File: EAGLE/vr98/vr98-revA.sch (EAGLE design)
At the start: 310 parts, among them U1 STM32F411CEU7

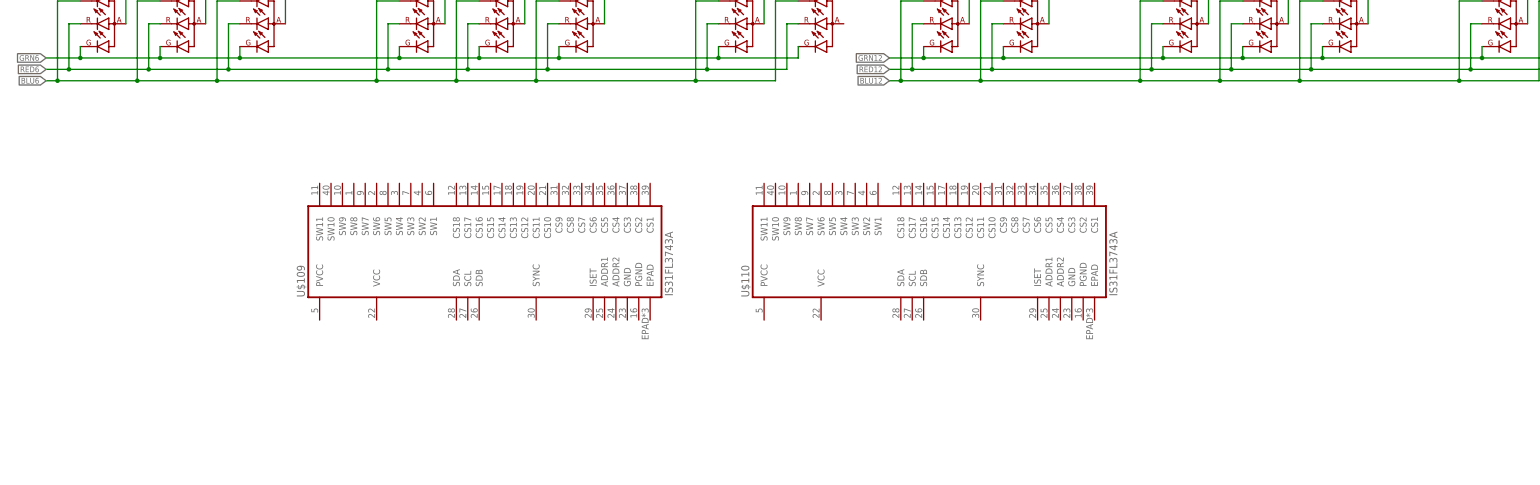
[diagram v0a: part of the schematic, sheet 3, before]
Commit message: led matrix done
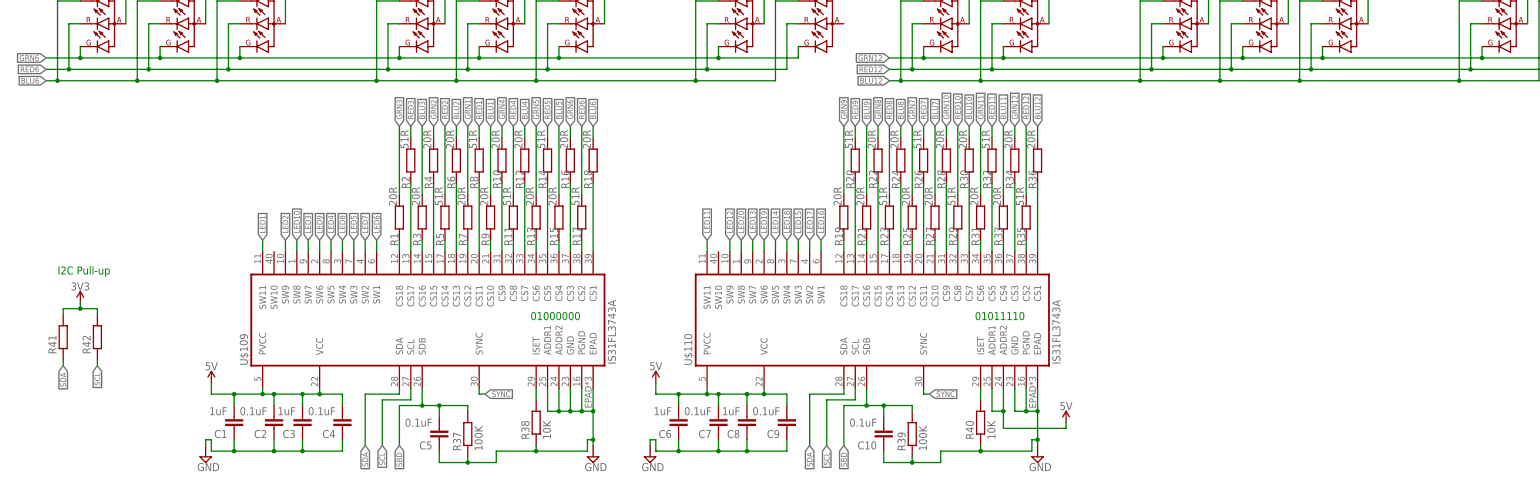
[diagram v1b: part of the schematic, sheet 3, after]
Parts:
- added C1, C3, C6, C8: 1uF, rcl:C-EUC0603
- added C10, C2, C4, C5, C7, C9: 0.1uF, rcl:C-EUC0603
- added R1, R10, R12, R13, R15, R16, R18, R19, R21, R22, R24, R25, R27, R28, R3, R30, R31, R33, R34, R36, R4, R6, R7, R9: 20R, rcl:R-EU_R0603
- added R11, R14, R17, R2, R20, R23, R26, R29, R32, R35, R5, R8: 51R, rcl:R-EU_R0603
- added R37, R39: 100K, rcl:R-EU_R0603
- added R38, R40: 10K, rcl:R-EU_R0603
- added R41, R42: (no value), rcl:R-EU_R0603
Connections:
- new net GND: C1.1, C10.1, C2.1, C3.1, C4.1, C5.1, C6.1, C7.1, C8.1, C9.1, R37.1, R38.1, R39.1, R40.1, U$109.ADDR1, U$109.ADDR2, U$109.EPAD, U$109.GND, U$109.PGND, U$110.EPAD, U$110.GND, U$110.PGND
- new net N$10: R29.1, U$110.CS8
- new net N$11: R28.1, U$110.CS9
- new net N$12: R27.1, U$110.CS10
- new net N$123: R14.1, U$109.CS5
- new net N$124: R13.1, U$109.CS6
- new net N$125: R12.1, U$109.CS7
- new net N$126: R11.1, U$109.CS8
- new net N$127: R10.1, U$109.CS9
- new net N$128: R9.1, U$109.CS10
- new net N$129: R8.1, U$109.CS11
- new net N$13: R26.1, U$110.CS11
- new net N$130: R7.1, U$109.CS12
- new net N$131: R5.1, U$109.CS14
- new net N$132: R4.1, U$109.CS15
- new net N$133: R3.1, U$109.CS16
- new net N$134: R2.1, U$109.CS17
- new net N$135: R1.1, U$109.CS18
- new net N$136: R38.2, U$109.ISET
- new net N$137: R40.2, U$110.ISET
- new net N$14: R25.1, U$110.CS12
- new net N$15: R23.1, U$110.CS14
- new net N$153: R6.1, U$109.CS13
- new net N$16: R22.1, U$110.CS15
- new net N$17: R21.1, U$110.CS16
- new net N$18: R20.1, U$110.CS17
- new net N$19: R19.1, U$110.CS18
- new net N$20: R24.1, U$110.CS13
- new net N$21: R18.1, U$109.CS1
- new net N$22: R17.1, U$109.CS2
- new net N$23: R16.1, U$109.CS3
- new net N$24: R15.1, U$109.CS4
- new net N$3: R36.1, U$110.CS1
- new net N$4: R35.1, U$110.CS2
- new net N$5: R34.1, U$110.CS3
- new net N$6: R33.1, U$110.CS4
- new net N$7: R32.1, U$110.CS5
- new net N$8: R31.1, U$110.CS6
- new net N$9: R30.1, U$110.CS7
- new net SBD: C10.2, C5.2, R37.2, R39.2, U$109.SDB, U$110.SDB
- new net SCL: R42.1, U$109.SCL, U$110.SCL
- new net SDA: R41.1, U$109.SDA, U$110.SDA
- new net SYNC: U$109.SYNC, U$110.SYNC
- new net VCC_1: C1.2, C2.2, C3.2, C4.2, C6.2, C7.2, C8.2, C9.2, U$109.PVCC, U$109.VCC, U$110.ADDR1, U$110.ADDR2, U$110.PVCC, U$110.VCC
- new net VCC_2: R41.2, R42.2
- net BLU1: now also R9.2
- net BLU10: now also R30.2
- net BLU11: now also R33.2
- net BLU12: now also R36.2
- net BLU2: now also R6.2
- net BLU3: now also R3.2
- net BLU4: now also R12.2
- net BLU5: now also R15.2
- net BLU6: now also R18.2
- net BLU7: now also R27.2
- net BLU8: now also R24.2
- net BLU9: now also R21.2
- net GRN1: now also R7.2
- net GRN10: now also R28.2
- net GRN11: now also R31.2
- net GRN12: now also R34.2
- net GRN2: now also R4.2
- net GRN3: now also R1.2
- net GRN4: now also R10.2
- net GRN5: now also R13.2
- net GRN6: now also R16.2
- net GRN7: now also R25.2
- net GRN8: now also R22.2
- net GRN9: now also R19.2
- net LED1: now also U$109.SW11
- net LED10: now also U$109.SW8
- net LED11: now also U$110.SW11
- net LED12: now also U$110.SW9
- net LED13: now also U$110.SW7
- net LED14: now also U$110.SW5
- net LED15: now also U$110.SW3
- net LED16: now also U$110.SW1
- net LED17: now also U$110.SW2
- net LED18: now also U$110.SW4
- net LED19: now also U$110.SW6
- net LED2: now also U$109.SW9
- net LED20: now also U$110.SW8
- net LED3: now also U$109.SW7
- net LED4: now also U$109.SW5
- net LED5: now also U$109.SW3
- net LED6: now also U$109.SW1
- net LED7: now also U$109.SW2
- net LED8: now also U$109.SW4
- net LED9: now also U$109.SW6
- net RED1: now also R8.2
- net RED10: now also R29.2
- net RED11: now also R32.2
- net RED12: now also R35.2
- net RED2: now also R5.2
- net RED3: now also R2.2
- net RED4: now also R11.2
- net RED5: now also R14.2
- net RED6: now also R17.2
- net RED7: now also R26.2
- net RED8: now also R23.2
- net RED9: now also R20.2
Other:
- note added: "01000000"
- note added: "01011110"
- note added: "I2C Pull-up"
- moved on the sheet: U$109, U$110

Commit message: wip
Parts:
- added C11: 22uF, rcl:C-EUC0603
- added C12, C13, C14, C15: 100nF, rcl:C-EUC0603
- added C16, C17, C18, C19: (no value), rcl:C-EUC0603
- added C20, C21, C25, C26, C27: 100nF, SparkFun-Capacitors:0.1UF-0603-25V-5%
- added C22, C23: 22uF, SparkFun-Capacitors:0.22UF-0603-25V-10%
- added C24: 4.7uF, SparkFun-Capacitors:1.0NF/1000PF-0603-50V-10%
- added D00: B5819W SL, jlcpcb_basic_parts:1N5819WS
- added D101, D102, D103: (no value), jlcpcb_basic_parts:1N5819WS
- added J1: (no value), ts_keyboards:UBD-C3
- added J2: (no value), ts_keyboards:UBD-S1_C4
- added L1: 10uH ±10%, rcl:L-USL3225M
- added LM1117: AMS1117-3.3, SparkFun-IC-Power:V_REG_LM1117SOT223
- added R43, R44: 5.1K, rcl:R-EU_R0603
- added R45, R46: 10R, rcl:R-EU_R0603
- added SW_CL_2, SW_SPC_2, SW_SPC_3: MX-5-PIN-MILMAX-3305-XNO-SILK, ts_keyboards:MX-5-PIN-MILMAX-3305-XNO-SILK
- added SW_DP_2, SW_ENT_2, SW_F17_2, SW_LS_2, SW_NUBS: MX-5-PIN-HOTSWAP-PADNO-SILK, ts_keyboards:MX-5-PIN-HOTSWAP-PADNO-SILK
- added U$108: DNP, ts_keyboards:156120M173000
- added U$111: M25C, ts_kb_mcu:M25C
- added U2, U3, U4: 74HC595PW, __untitled:74HC595PW
- added Y1: 32.768kHz ±20ppm 6pF, SparkFun-Clocks:CRYSTAL-32.768KHZSMD-3.2X1.5
- added Y2: 25MHz 9pF, SparkFun-Clocks:CRYSTAL-24MHZ"
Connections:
- net N$79 renamed K_CL
- new net ENC_A: R44.1, SW_F17.A, U1A.PA8
- new net ENC_B: R43.1, SW_F17.B, U1A.PA9
- new net K_DP: D50.A, SW_DP.P, SW_DP_2.P
- new net K_ENT: D67.A, SW_ENT.P, SW_ENT_2.P
- new net K_F13: D18.A, SW_F17.D, SW_F17_2.P
- new net K_LS: D71.A, SW_CL_2.P, SW_LS.P, SW_LS_2.P
- new net MISO: U1A.PA6
- new net MOSI: U1A.PA7
- new net N$138: C18.1, U1A.PH0-OSC_IN, Y2.2
- new net N$139: C19.1, U1A.PH1-OSC_OUT, Y2.1
- new net N$140: R45.2, U1A.PA11
- new net N$141: R46.2, U1A.PA12
- new net N$142: D101.A, SW_NUBS.P
- new net N$154: D102.A, SW_SPC_2.P
- new net N$155: D103.A, SW_SPC_3.P
- new net N$79: C16.1, U1A.PC14-OSC32_IN, Y1.2
- new net SCKL: U1A.PA5
- new net UDB_DP: R46.1
- new net USB_DN: J1.D-, J2.D-, R45.1
- new net USB_DP: J1.D+, J2.D+
- net BLU7: now also U$108.B
- net COL0: now also SW_CL_2.S, SW_LS_2.S
- net COL1: now also SW_NUBS.S
- net COL13: now also SW_DP_2.S, SW_ENT_2.S
- net COL17: now also SW_F17_2.S
- net COL3: now also SW_SPC_2.S
- net COL7: now also SW_SPC_3.S
- net GND: now also C11.2, C12.2, C13.2, C14.2, C15.2, C16.2, C17.2, C18.2, C19.2, C20.2, C21.2, C22.2, C23.2, C24.2, J1.GND, J2.GND, LM1117.ADJ, SW_F17.1, SW_F17.2, SW_F17.C, U1B.EPAD, U1B.VSS, U1B.VSSA, U1B.VSS_2, U1B.VSS_3
- net GRN7: now also U$108.G
- net LED20: now also U$108.A
- net N$1: now also L1.1, U1B.VREF+; no longer D71.A, SW_LS.P
- net N$122: now also C17.1, U1A.PC15-OSC32_OUT, Y1.1; no longer D18.A, SW_F17.D
- net N$70: now also C13.1, C14.1, C15.1; no longer D50.A, SW_DP.P
- net N$75: now also C11.1, U1B.VCAP1; no longer D67.A, SW_ENT.P
- net RED7: now also U$108.R
- net ROW4: now also D101.C
- net ROW5: now also D102.C, D103.C
- net SCL: now also U1A.PB6
- net SDA: now also U1A.PB7
- net VCC_1: now also C21.1, C23.1, D00.C, J1.VCC, J2.VCC, LM1117.IN
- net VCC_2: now also C12.1, C20.1, C22.1, C24.1, D00.A, L1.2, LM1117.OUT, R43.2, R44.2, U1B.VDD, U1B.VDD_2, U1B.VDD_3
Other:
- note added: "** NEW ** Unified Daughter Board (C4) Conn."
- note added: "DNP"
- note added: "DNP Unified Daughter Board (C3) Conn."
- moved on the sheet: U1A, U1B

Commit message: wip
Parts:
- removed SW_F17_2: MX-5-PIN-HOTSWAP-PADNO-SILK, ts_keyboards:MX-5-PIN-HOTSWAP-PADNO-SILK
- removed U$111: M25C, ts_kb_mcu:M25C
- added C28: 100nF, SparkFun-Capacitors:0.1UF-0603-25V-5%
- added C29: (no value), rcl:C-EUC0603
- added C30: 100nF, rcl:C-EUC0805
- added C31: 100nF, rcl:C-EUC0603
- added D104: (no value), jlcpcb_basic_parts:1N5819WS
- added D107: BLUE, SparkFun-LED:LED-BLUE0603
- added D201, D202: 1N4148, adafruit:DIODESOT23_REFLOW
- added JI2C, JPWM: (no value), SparkFun-Connectors:CONN_04
- added JKEY: (no value), __untitled:MOLEX_0781710004
- added JSPI: DNP, SparkFun-Connectors:AVR_SPI_PROG_3X2NS
- added JSPI@2: (no value), SparkFun-Connectors:CONN_01
- added JTAG: DNP, SparkFun-Connectors:CONN_05X2NO_SILK
- added J_5V: 5V SRC SELECT, SparkFun-Jumpers:JUMPER-SMT_3_1-NC_TRACE_SILK
- added Q1: 2N7002, adafruit:MOSFET-NREFLOW
- added Q2: DMG2305UX-7, SparkFun-DiscreteSemi:MOSFET_PCH-DMG2305UX-7
- added Q3: IRLML6401, SparkFun-DiscreteSemi:MOSFET_PCH-IRLML2244
- added Q4: 2N2222, SparkFun-DiscreteSemi:TRANS_NPN-MMBT2222AL
- added R47, R48, R49, R50, R51, R52, R53, R54, R55, R56, R57, R58, R59, R60, R61, R62, R63, R64, R66: 10K, rcl:R-EU_R0603
- added R65: 5.1K, rcl:R-EU_R0603
- added R67, R68, R71, R73: 100K, rcl:R-EU_R0603
- added R69: /DNP/, rcl:R-EU_R0603
- added R70, R72: 1K, rcl:R-EU_R0603
- added S1: Reset, SparkFun-Switches:MOMENTARY-SWITCH-SPST-SMD-5.2-TALL-REDUNDANT
- added S2: KEY, SparkFun-Switches:MOMENTARY-SWITCH-SPST-SMD-5.2-TALL-REDUNDANT
- added SW_F13_2: MX-5-PIN-HOTSWAP-PADNO-SILK, ts_keyboards:MX-5-PIN-HOTSWAP-PADNO-SILK
- added U5: M25C, ts_kb_mcu:M25C
- C16, C17: value (none) -> 4.3pF
- C18, C19: value (none) -> 12pF
- D102: value (none) -> DNP
- U2, U3, U4: value 74HC595PW -> 74HC589A_DT; device __untitled:74HC595PW -> __untitled:74HC589A_DT
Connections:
- net N$54 renamed K_BSP
- removed net N$1: L1.1, U1B.VREF+
- removed net SCKL: U1A.PA5
- new net !BOOT: C30.1, D202.A, Q2.G, R67.1
- new net !RESET: C29.2, D201.A, R69.1, U1A.NRST
- new net 5V_SELECT: C1.2, C2.2, C3.2, C4.2, C6.2, C7.2, C8.2, C9.2, J_5V.2, U$109.PVCC, U$109.VCC, U$110.ADDR1, U$110.ADDR2, U$110.PVCC, U$110.VCC
- new net AUX_CS: JSPI.5, U1A.PB1
- new net AUX_DC: JSPI@2.1, U1A.PA1
- new net BOOT0: Q2.D, R68.1, U1A.BOOT0
- new net BOOT1: R66.2, U1A.PB2
- new net CK/DATA/PWM: JPWM.3, U1A.PA8
- new net EE_CS: U1A.PB0, U5.!CS
- new net GND2: R47.1, R48.1, R49.1, R50.1, R51.1, R52.1, R53.1, R54.1, R55.1, R56.1, R57.1, R58.1, R59.1, R60.1, R61.1, R62.1, R63.1, R64.1
- new net J_RST: JTAG.10, U1A.PB4
- new net J_TCK: JTAG.4, U1A.PA14
- new net J_TDI: JTAG.8, U1A.PA15
- new net J_TDO: JTAG.6, U1A.PB3
- new net J_TMS: JTAG.2, U1A.PA13
- new net LATCH: Q1.D, R65.1, U2.LATCH, U2.SS/!PL, U3.LATCH, U3.SS/!PL, U4.LATCH, U4.SS/!PL
- new net LED: D107.C, U1A.PC13-ANTI_TAMP
- new net LED_EN: R73.2, U1A.PB10
- new net LED_VCC: C31.1, J_5V.1, Q3.D
- new net MATRIX_CS: Q1.G, U1A.PA4, U2.OE/!CS, U3.OE/!CS, U4.OE/!CS
- new net N$143: C12.1, L1.1, U1B.VREF+
- new net N$144: D102.A, JKEY.3, S2.1
- new net N$145: D107.A, R70.2
- new net N$146: D201.C, D202.C, S1.2
- new net N$147: Q4.C, R72.1
- new net N$148: C31.2, Q3.G, R71.1, R72.2
- new net N$149: U3.QH, U4.SA
- new net N$162: U2.QH, U3.SA
- new net N$54: Q1.S
- new net RX: U1A.PA10
- new net SCK: JSPI.3, U1A.PA5, U2.SC/SCK, U3.SC/SCK, U4.SC/SCK, U5.CLK
- new net TX: U1A.PA9
- new net WKUP: U1A.PA0-WKUP
- net COL0: now also D1.C, D19.C, D37.C, D55.C, D71.C, D88.C, R47.2, U2.B; no longer SW_CL.S, SW_CL_2.S, SW_ESC.S, SW_LC.S, SW_LS.S, SW_LS_2.S, SW_TAB.S, SW_TDL.S
- net COL1: now also D2.C, D20.C, D38.C, D56.C, D89.C, R48.2, U2.C; no longer SW_1.S, SW_A.S, SW_F1.S, SW_LW.S, SW_NUBS.S, SW_Q.S
- net COL10: now also D11.C, D29.C, D47.C, D65.C, D80.C, D95.C, R57.2, U3.F; no longer SW_0.S, SW_CS.S, SW_DT.S, SW_F10.S, SW_P.S, SW_RC.S
- net COL11: now also D12.C, D30.C, D48.C, D66.C, D81.C, R58.2, U3.G; no longer SW_F11.S, SW_FN.S, SW_FS.S, SW_MU.S, SW_OB.S, SW_QU.S
- net COL12: now also D13.C, D31.C, D49.C, D82.C, D96.C, R59.2, U4.B; no longer SW_CB.S, SW_EP.S, SW_F12.S, SW_LF.S, SW_RS.S
- net COL13: now also D14.C, D32.C, D50.C, D67.C, D83.C, D97.C, R60.2, SW_DP_2.P, SW_ENT_2.P, U4.C; no longer SW_BSP.S, SW_DN.S, SW_DP.S, SW_DP_2.S, SW_ENT.S, SW_ENT_2.S, SW_F13.S, SW_UP.S
- net COL14: now also D15.C, D33.C, D51.C, D68.C, D84.C, D98.C, R61.2, U4.D; no longer SW_F14.S, SW_N1.S, SW_N4.S, SW_N7.S, SW_NUM.S, SW_RT.S
- net COL15: now also D16.C, D34.C, D52.C, D69.C, D85.C, D99.C, R62.2, U4.E; no longer SW_DSH.S, SW_F15.S, SW_N0.S, SW_N2.S, SW_N5.S, SW_N8.S
- net COL16: now also D100.C, D17.C, D35.C, D53.C, D70.C, D86.C, R63.2, U4.F; no longer SW_F16.S, SW_MUL.S, SW_N3.S, SW_ND.S
- net COL17: now also D18.C, D36.C, D54.C, D87.C, R64.2, SW_F13_2.P, U4.G; no longer SW_F17.E, SW_F17_2.S, SW_MIN.S, SW_NEN.S, SW_NP.S
- net COL2: now also D101.C, D21.C, D3.C, D39.C, D57.C, D72.C, D90.C, R49.2, U2.D; no longer SW_2.S, SW_F2.S, SW_LA.S, SW_S.S, SW_W.S, SW_Z.S
- net COL3: now also D103.C, D22.C, D4.C, D40.C, D58.C, D73.C, R50.2, U2.E; no longer SW_3.S, SW_D.S, SW_E.S, SW_F3.S, SW_SPC_2.S, SW_X.S
- net COL4: now also D102.C, D23.C, D41.C, D5.C, D59.C, D74.C, R51.2, U2.F; no longer SW_4.S, SW_C.S, SW_F.S, SW_F4.S, SW_R.S
- net COL5: now also D24.C, D42.C, D6.C, D60.C, D75.C, D91.C, R52.2, U2.G; no longer SW_5.S, SW_F5.S, SW_G.S, SW_SPC.S, SW_T.S, SW_V.S
- net COL6: now also D104.C, D25.C, D43.C, D61.C, D7.C, D76.C, R53.2, U3.B; no longer SW_6.S, SW_B.S, SW_F6.S, SW_H.S, SW_Y.S
- net COL7: now also D26.C, D44.C, D62.C, D77.C, D8.C, D92.C, R54.2, U3.C; no longer SW_7.S, SW_F7.S, SW_J.S, SW_N.S, SW_SPC_3.S, SW_U.S
- net COL8: now also D27.C, D45.C, D63.C, D78.C, D9.C, D93.C, R55.2, U3.D; no longer SW_8.S, SW_F8.S, SW_I.S, SW_K.S, SW_M.S, SW_RA.S
- net COL9: now also D10.C, D28.C, D46.C, D64.C, D79.C, D94.C, R56.2, U3.E; no longer SW_9.S, SW_CM.S, SW_F9.S, SW_L.S, SW_O.S, SW_RW.S
- net ENC_A: now also U1A.PA2; no longer U1A.PA8
- net ENC_B: now also U1A.PA3; no longer U1A.PA9
- net GND: now also C25.2, C26.2, C27.2, C28.2, C29.1, C30.2, JI2C.4, JKEY.4, JPWM.4, JSPI.6, JTAG.3, JTAG.5, JTAG.9, Q4.E, R66.1, R68.2, S1.1, U1B.VBAT, U2.A, U2.GND, U2.H, U2.SA, U3.A, U3.GND, U3.H, U4.A, U4.GND, U4.H, U5.GND
- net K_CL: now also SW_CL_2.P
- net K_DP: now also SW_DP_2.S; no longer SW_DP_2.P
- net K_ENT: now also SW_ENT_2.S; no longer SW_ENT_2.P
- net K_F13: now also SW_F13_2.S; no longer SW_F17_2.P
- net K_LS: no longer SW_CL_2.P
- net LED10: now also U$100.A
- net MISO: now also JSPI.1, U4.QH, U5.DO
- net MOSI: now also JSPI.4, U5.DIO
- net N$154: now also D103.A; no longer D102.A
- net N$155: now also D104.A; no longer D103.A
- net N$70: now also Q4.B, R73.1; no longer C13.1, C14.1, C15.1
- net ROW0: now also SW_ESC.S, SW_F1.S, SW_F10.S, SW_F11.S, SW_F12.S, SW_F13.S, SW_F14.S, SW_F15.S, SW_F16.S, SW_F17.E, SW_F2.S, SW_F3.S, SW_F4.S, SW_F5.S, SW_F6.S, SW_F7.S, SW_F8.S, SW_F9.S, U1A.PB12; no longer D1.C, D10.C, D11.C, D12.C, D13.C, D14.C, D15.C, D16.C, D17.C, D18.C, D2.C, D3.C, D4.C, D5.C, D6.C, D7.C, D8.C, D9.C
- net ROW1: now also SW_0.S, SW_1.S, SW_2.S, SW_3.S, SW_4.S, SW_5.S, SW_6.S, SW_7.S, SW_8.S, SW_9.S, SW_BSP.S, SW_DSH.S, SW_EP.S, SW_MIN.S, SW_MU.S, SW_MUL.S, SW_NUM.S, SW_TDL.S, U1A.PB13; no longer D19.C, D20.C, D21.C, D22.C, D23.C, D24.C, D25.C, D26.C, D27.C, D28.C, D29.C, D30.C, D31.C, D32.C, D33.C, D34.C, D35.C, D36.C
- net ROW2: now also SW_CB.S, SW_DP.S, SW_E.S, SW_I.S, SW_N7.S, SW_N8.S, SW_N9.S, SW_NP.S, SW_O.S, SW_OB.S, SW_P.S, SW_Q.S, SW_R.S, SW_T.S, SW_TAB.S, SW_U.S, SW_W.S, SW_Y.S, U1A.PB14; no longer D37.C, D38.C, D39.C, D40.C, D41.C, D42.C, D43.C, D44.C, D45.C, D46.C, D47.C, D48.C, D49.C, D50.C, D51.C, D52.C, D53.C, D54.C
- net ROW3: now also SW_A.S, SW_CL.S, SW_CL_2.S, SW_CS.S, SW_D.S, SW_ENT.S, SW_F.S, SW_G.S, SW_H.S, SW_J.S, SW_K.S, SW_L.S, SW_N4.S, SW_N5.S, SW_N6.S, SW_QU.S, SW_S.S, U1A.PB15; no longer D55.C, D56.C, D57.C, D58.C, D59.C, D60.C, D61.C, D62.C, D63.C, D64.C, D65.C, D66.C, D67.C, D68.C, D69.C, D70.C
- net ROW4: now also SW_B.S, SW_C.S, SW_CM.S, SW_DT.S, SW_FS.S, SW_LS.S, SW_LS_2.S, SW_M.S, SW_N.S, SW_N1.S, SW_N2.S, SW_N3.S, SW_NEN.S, SW_NUBS.S, SW_RS.S, SW_UP.S, SW_V.S, SW_X.S, SW_Z.S, U1A.PB8; no longer D101.C, D71.C, D72.C, D73.C, D74.C, D75.C, D76.C, D77.C, D78.C, D79.C, D80.C, D81.C, D82.C, D83.C, D84.C, D85.C, D86.C, D87.C
- net ROW5: now also JKEY.2, S2.2, SW_DN.S, SW_FN.S, SW_LA.S, SW_LC.S, SW_LF.S, SW_LW.S, SW_N0.S, SW_ND.S, SW_RA.S, SW_RC.S, SW_RT.S, SW_RW.S, SW_SPC.S, SW_SPC_2.S, SW_SPC_3.S, U1A.PB9; no longer D100.C, D102.C, D103.C, D88.C, D89.C, D90.C, D91.C, D92.C, D93.C, D94.C, D95.C, D96.C, D97.C, D98.C, D99.C
- net SCL: now also JI2C.1
- net SDA: now also JI2C.2
- net VCC_1: now also JPWM.1, J_5V.3, Q3.S, R71.2; no longer C1.2, C2.2, C3.2, C4.2, C6.2, C7.2, C8.2, C9.2, U$109.PVCC, U$109.VCC, U$110.ADDR1, U$110.ADDR2, U$110.PVCC, U$110.VCC
- net VCC_2: now also C13.1, C14.1, C15.1, C25.1, C26.1, C27.1, C28.1, JI2C.3, JKEY.1, JPWM.2, JSPI.2, JTAG.1, Q2.S, R65.2, R67.2, R69.2, R70.1, U2.VCC, U3.VCC, U4.VCC, U5.!HLD, U5.!WP, U5.VCC; no longer C12.1
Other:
- note added: "!RESET"
- note added: "(SW_NEN_2)"
- note added: "(SW_NP_2)"
- note added: "5V to 3V3 Power Circuit"
- note added: "BOOT0 Inversion"
- note added: "BOOT1"
- note added: "COL-SCAN PULL-DOWNS"
- note added: "Column Scanner Shift Registers"
- note added: "DIP_SWITCH"
- note added: "ISO KEY SET"
- note added: "JIS VARIENT (SW_BSP_2)"
- note added: "JIS VARIENT (SW_RS_2)"
- note added: "JIS VARIENT SW_SPC_2"
- note added: "JIS VARIENT SW_SPC_3"
- note added: "LED POWER SWITCH /DNP/ (Optional)"
- note added: "Optional DIP Switch"
- note added: "SPI EEPROM (Optional)"
- note added: "SPLIT SPACE"
- note added: "STEP CAPS-LOCK"
- note added: "STM32F411 MCU"
- note added: "STM32F411 MCU (Power)"
- note added: "SW_NUBS"
- note added: "Status LED"
- moved on the sheet: C1, C10, C11, C12, C13, C14, C15, C2, C25, C26, C27, C3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
